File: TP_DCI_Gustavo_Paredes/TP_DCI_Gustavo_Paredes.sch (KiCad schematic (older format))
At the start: 30 parts, among them U101 LTC1485IS8PBF, U102 LTC1485IS8PBF, X701DB9F/101 DB9_Female, X702DB9M/101 DB9_Male

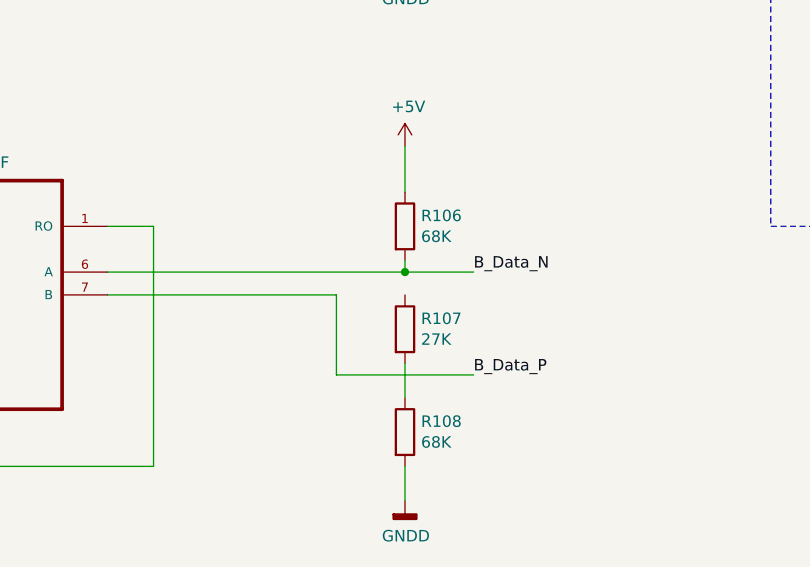
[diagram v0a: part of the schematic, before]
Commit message: Coneccion faltante.
Agregue una pequeña conexión faltante.
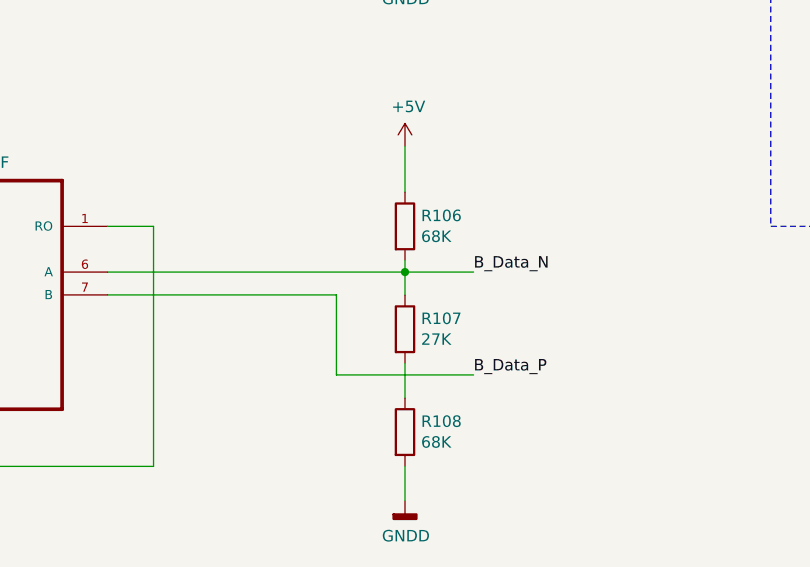
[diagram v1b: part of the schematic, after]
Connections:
- wire segments 150 -> 151
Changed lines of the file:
@@
 	0    -1   -1   0
 $EndComp
+Wire Wire Line
+	6300 3800 6300 3700
 Wire Bus Line
 	2250 1000 2250 4300

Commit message: Arreglo Etiqueta Global
Arregle la etiqueta global para que pase el ERC. Pero sigo con problemas en otros puntos.
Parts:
- C101, C102: footprint (none) -> Capacitor_THT:C_Disc_D3.0mm_W2.0mm_P2.50mm
- D101, D103, D104, D106, D107, D109, D110, D112: footprint (none) -> Diode_THT:D_DO-34_SOD68_P7.62mm_Horizontal
- D102, D105: footprint (none) -> Package_TO_SOT_SMD:SOT-23
- R101, R102, R103, R104, R105, R106, R107, R108, R109, R110, R111, R112: footprint (none) -> Resistor_THT:R_Axial_DIN0204_L3.6mm_D1.6mm_P5.08mm_Horizontal
- U101, U102: footprint SOIC127P600X175-8N -> LTC1485IS8PBF:SOIC127P600X175-8N
- X701DB9F/101: footprint (none) -> Connector_Dsub:DSUB-9_Female_Horizontal_P2.77x2.84mm_EdgePinOffset4.94mm_Housed_MountingHolesOffset7.48mm
- X702DB9M/101: footprint (none) -> Connector_Dsub:DSUB-9_Male_Horizontal_P2.77x2.84mm_EdgePinOffset4.94mm_Housed_MountingHolesOffset7.48mm
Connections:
- wire segments 151 -> 159
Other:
- note added: "Etiqueta Global\npara corregir ERC."
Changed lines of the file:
@@
 F 0 "X701DB9F/101" H 8520 1108 50  0000 C CNN
 F 1 "DB9_Female" H 8520 1199 50  0000 C CNN
-F 2 "" H 8600 1800 50  0001 C CNN
+F 2 "Connector_Dsub:DSUB-9_Female_Horizontal_P2.77x2.84mm_EdgePinOffset4.94mm_Housed_MountingHolesOffset7.48mm" H 8600 1800 50  0001 C CNN
 F 3 " ~" H 8600 1800 50  0001 C CNN
 	1    8600 1800
@@
 F 0 "R109" V 8843 2650 50  0000 C CNN
 F 1 "10R" V 8934 2650 50  0000 C CNN
-F 2 "" V 8980 2650 50  0001 C CNN
+F 2 "Resistor_THT:R_Axial_DIN0204_L3.6mm_D1.6mm_P5.08mm_Horizontal" V 8980 2650 50  0001 C CNN
 F 3 "~" H 9050 2650 50  0001 C CNN
 	1    9050 2650
@@
 F 0 "R111" V 9643 2650 50  0000 C CNN
 F 1 "10R" V 9734 2650 50  0000 C CNN
-F 2 "" V 9780 2650 50  0001 C CNN
+F 2 "Resistor_THT:R_Axial_DIN0204_L3.6mm_D1.6mm_P5.08mm_Horizontal" V 9780 2650 50  0001 C CNN
 F 3 "~" H 9850 2650 50  0001 C CNN
 	1    9850 2650
@@
 F 0 "R110" V 8843 3000 50  0000 C CNN
 F 1 "10R" V 8934 3000 50  0000 C CNN
-F 2 "" V 8980 3000 50  0001 C CNN
+F 2 "Resistor_THT:R_Axial_DIN0204_L3.6mm_D1.6mm_P5.08mm_Horizontal" V 8980 3000 50  0001 C CNN
 F 3 "~" H 9050 3000 50  0001 C CNN
 	1    9050 3000
@@
 F 0 "R112" V 9643 3000 50  0000 C CNN
 F 1 "10R" V 9734 3000 50  0000 C CNN
-F 2 "" V 9780 3000 50  0001 C CNN
+F 2 "Resistor_THT:R_Axial_DIN0204_L3.6mm_D1.6mm_P5.08mm_Horizontal" V 9780 3000 50  0001 C CNN
 F 3 "~" H 9850 3000 50  0001 C CNN
 	1    9850 3000
@@
 F 0 "R103" H 6370 1246 50  0000 L CNN
 F 1 "68K" H 6370 1155 50  0000 L CNN
-F 2 "" V 6230 1200 50  0001 C CNN
+F 2 "Resistor_THT:R_Axial_DIN0204_L3.6mm_D1.6mm_P5.08mm_Horizontal" V 6230 1200 50  0001 C CNN
 F 3 "~" H 6300 1200 50  0001 C CNN
 	1    6300 1200
@@
 F 0 "R104" H 6370 1696 50  0000 L CNN
 F 1 "27K" H 6370 1605 50  0000 L CNN
-F 2 "" V 6230 1650 50  0001 C CNN
+F 2 "Resistor_THT:R_Axial_DIN0204_L3.6mm_D1.6mm_P5.08mm_Horizontal" V 6230 1650 50  0001 C CNN
 F 3 "~" H 6300 1650 50  0001 C CNN
 	1    6300 1650
@@
 F 0 "R105" H 6370 2096 50  0000 L CNN
 F 1 "68K" H 6370 2005 50  0000 L CNN
-F 2 "" V 6230 2050 50  0001 C CNN
+F 2 "Resistor_THT:R_Axial_DIN0204_L3.6mm_D1.6mm_P5.08mm_Horizontal" V 6230 2050 50  0001 C CNN
 F 3 "~" H 6300 2050 50  0001 C CNN
 	1    6300 2050
@@
 F 0 "R106" H 6370 3546 50  0000 L CNN
 F 1 "68K" H 6370 3455 50  0000 L CNN
-F 2 "" V 6230 3500 50  0001 C CNN
+F 2 "Resistor_THT:R_Axial_DIN0204_L3.6mm_D1.6mm_P5.08mm_Horizontal" V 6230 3500 50  0001 C CNN
 F 3 "~" H 6300 3500 50  0001 C CNN
 	1    6300 3500
@@
 F 0 "R107" H 6370 3996 50  0000 L CNN
 F 1 "27K" H 6370 3905 50  0000 L CNN
-F 2 "" V 6230 3950 50  0001 C CNN
+F 2 "Resistor_THT:R_Axial_DIN0204_L3.6mm_D1.6mm_P5.08mm_Horizontal" V 6230 3950 50  0001 C CNN
 F 3 "~" H 6300 3950 50  0001 C CNN
 	1    6300 3950
@@
 F 0 "R108" H 6370 4446 50  0000 L CNN
 F 1 "68K" H 6370 4355 50  0000 L CNN
-F 2 "" V 6230 4400 50  0001 C CNN
+F 2 "Resistor_THT:R_Axial_DIN0204_L3.6mm_D1.6mm_P5.08mm_Horizontal" V 6230 4400 50  0001 C CNN
 F 3 "~" H 6300 4400 50  0001 C CNN
 	1    6300 4400
@@
 F 0 "X702DB9M/101" H 10070 1108 50  0000 C CNN
 F 1 "DB9_Male" H 10070 1199 50  0000 C CNN
-F 2 "" H 10150 1800 50  0001 C CNN
+F 2 "Connector_Dsub:DSUB-9_Male_Horizontal_P2.77x2.84mm_EdgePinOffset4.94mm_Housed_MountingHolesOffset7.48mm" H 10150 1800 50  0001 C CNN
 F 3 " ~" H 10150 1800 50  0001 C CNN
 	1    10150 1800
@@
 F 0 "D104" V 3396 6471 50  0000 R CNN
 F 1 "4,7V" V 3305 6471 50  0000 R CNN
-F 2 "" H 3350 6550 50  0001 C CNN
+F 2 "Diode_THT:D_DO-34_SOD68_P7.62mm_Horizontal" H 3350 6550 50  0001 C CNN
 F 3 "~" H 3350 6550 50  0001 C CNN
 	1    3350 6550
@@
 F 0 "D106" V 3804 6629 50  0000 L CNN
 F 1 "8,2V" V 3895 6629 50  0000 L CNN
-F 2 "" H 3850 6550 50  0001 C CNN
+F 2 "Diode_THT:D_DO-34_SOD68_P7.62mm_Horizontal" H 3850 6550 50  0001 C CNN
 F 3 "~" H 3850 6550 50  0001 C CNN
 	1    3850 6550
@@
 F 0 "D105" V 3304 7028 50  0000 L CNN
 F 1 "BAV99" V 3395 7028 50  0000 L CNN
-F 2 "" H 3350 6950 50  0001 C CNN
+F 2 "Package_TO_SOT_SMD:SOT-23" H 3350 6950 50  0001 C CNN
 F 3 "~" H 3350 6950 50  0001 C CNN
 	2    3350 6950
@@
 F 0 "R101" H 3020 2046 50  0000 L CNN
 F 1 "10K" H 3020 1955 50  0000 L CNN
-F 2 "" V 2880 2000 50  0001 C CNN
+F 2 "Resistor_THT:R_Axial_DIN0204_L3.6mm_D1.6mm_P5.08mm_Horizontal" V 2880 2000 50  0001 C CNN
 F 3 "~" H 2950 2000 50  0001 C CNN
 	1    2950 2000
@@
 F 0 "C101" V 3198 1000 50  0000 C CNN
 F 1 "22nF" V 3289 1000 50  0000 C CNN
-F 2 "" H 3488 850 50  0001 C CNN
+F 2 "Capacitor_THT:C_Disc_D3.0mm_W2.0mm_P2.50mm" H 3488 850 50  0001 C CNN
 F 3 "~" H 3450 1000 50  0001 C CNN
 	1    3450 1000
@@
 F 0 "U101" H 4300 1970 50  0000 C CNN
 F 1 "LTC1485IS8PBF" H 4300 1879 50  0000 C CNN
-F 2 "SOIC127P600X175-8N" H 4300 1400 50  0001 L BNN
+F 2 "LTC1485IS8PBF:SOIC127P600X175-8N" H 4300 1400 50  0001 L BNN
 F 3 "SOIC-8 Analog Devices" H 4300 1400 50  0001 L BNN
 F 4 "LTC1485IS8#PBF" H 4300 1400 50  0001 L BNN "Field4"
@@
 F 0 "R102" H 3020 4346 50  0000 L CNN
 F 1 "10K" H 3020 4255 50  0000 L CNN
-F 2 "" V 2880 4300 50  0001 C CNN
+F 2 "Resistor_THT:R_Axial_DIN0204_L3.6mm_D1.6mm_P5.08mm_Horizontal" V 2880 4300 50  0001 C CNN
 F 3 "~" H 2950 4300 50  0001 C CNN
 	1    2950 4300
@@
 F 0 "C102" V 3198 3300 50  0000 C CNN
 F 1 "22nF" V 3289 3300 50  0000 C CNN
-F 2 "" H 3488 3150 50  0001 C CNN
+F 2 "Capacitor_THT:C_Disc_D3.0mm_W2.0mm_P2.50mm" H 3488 3150 50  0001 C CNN
 F 3 "~" H 3450 3300 50  0001 C CNN
 	1    3450 3300
@@
 F 0 "U102" H 4300 4270 50  0000 C CNN
 F 1 "LTC1485IS8PBF" H 4300 4179 50  0000 C CNN
-F 2 "SOIC127P600X175-8N" H 4300 3700 50  0001 L BNN
+F 2 "LTC1485IS8PBF:SOIC127P600X175-8N" H 4300 3700 50  0001 L BNN
 F 3 "SOIC-8 Analog Devices" H 4300 3700 50  0001 L BNN
 F 4 "LTC1485IS8#PBF" H 4300 3700 50  0001 L BNN "Field4"
@@
 F 0 "D101" V 2396 6471 50  0000 R CNN
 F 1 "4,7V" V 2305 6471 50  0000 R CNN
-F 2 "" H 2350 6550 50  0001 C CNN
+F 2 "Diode_THT:D_DO-34_SOD68_P7.62mm_Horizontal" H 2350 6550 50  0001 C CNN
 F 3 "~" H 2350 6550 50  0001 C CNN
 	1    2350 6550
@@
 F 0 "D103" V 2804 6629 50  0000 L CNN
 F 1 "8,2V" V 2895 6629 50  0000 L CNN
-F 2 "" H 2850 6550 50  0001 C CNN
+F 2 "Diode_THT:D_DO-34_SOD68_P7.62mm_Horizontal" H 2850 6550 50  0001 C CNN
 F 3 "~" H 2850 6550 50  0001 C CNN
 	1    2850 6550
@@
 F 0 "D102" V 2304 7028 50  0000 L CNN
 F 1 "BAV99" V 2395 7028 50  0000 L CNN
-F 2 "" H 2350 6950 50  0001 C CNN
+F 2 "Package_TO_SOT_SMD:SOT-23" H 2350 6950 50  0001 C CNN
 F 3 "~" H 2350 6950 50  0001 C CNN
 	2    2350 6950
@@
 F 0 "D102" V 2896 6862 50  0000 R CNN
 F 1 "BAV99" V 2805 6862 50  0000 R CNN
-F 2 "" H 2850 6950 50  0001 C CNN
+F 2 "Package_TO_SOT_SMD:SOT-23" H 2850 6950 50  0001 C CNN
 F 3 "~" H 2850 6950 50  0001 C CNN
 	1    2850 6950
@@
 F 0 "D110" V 5596 6471 50  0000 R CNN
 F 1 "4,7V" V 5505 6471 50  0000 R CNN
-F 2 "" H 5550 6550 50  0001 C CNN
+F 2 "Diode_THT:D_DO-34_SOD68_P7.62mm_Horizontal" H 5550 6550 50  0001 C CNN
 F 3 "~" H 5550 6550 50  0001 C CNN
 	1    5550 6550
@@
 F 0 "D112" V 6004 6629 50  0000 L CNN
 F 1 "8,2V" V 6095 6629 50  0000 L CNN
-F 2 "" H 6050 6550 50  0001 C CNN
+F 2 "Diode_THT:D_DO-34_SOD68_P7.62mm_Horizontal" H 6050 6550 50  0001 C CNN
 F 3 "~" H 6050 6550 50  0001 C CNN
 	1    6050 6550
@@
 B_Data_P
 Wire Wire Line
-	5550 7150 5800 7150
-Wire Wire Line
 	5550 6800 5550 6700
 Wire Wire Line
 	6050 6700 6050 6800
-Wire Wire Line
-	5800 7150 5800 7250
-Connection ~ 5800 7150
-Wire Wire Line
-	5800 7150 6050 7150
 Wire Wire Line
 	6050 6400 6050 5900
@@
 F 0 "D107" V 4596 6471 50  0000 R CNN
 F 1 "4,7V" V 4505 6471 50  0000 R CNN
-F 2 "" H 4550 6550 50  0001 C CNN
+F 2 "Diode_THT:D_DO-34_SOD68_P7.62mm_Horizontal" H 4550 6550 50  0001 C CNN
 F 3 "~" H 4550 6550 50  0001 C CNN
 	1    4550 6550
@@
 F 0 "D109" V 5004 6629 50  0000 L CNN
 F 1 "8,2V" V 5095 6629 50  0000 L CNN
-F 2 "" H 5050 6550 50  0001 C CNN
+F 2 "Diode_THT:D_DO-34_SOD68_P7.62mm_Horizontal" H 5050 6550 50  0001 C CNN
 F 3 "~" H 5050 6550 50  0001 C CNN
 	1    5050 6550
@@
 Wire Wire Line
 	6300 3800 6300 3700
+$Comp
+L power:GNDPWR #PWR0121
+U 1 1 5D13F9B9
+P 6650 2350
+F 0 "#PWR0121" H 6650 2150 50  0001 C CNN
+F 1 "GNDPWR" H 6654 2196 50  0000 C CNN
+F 2 "" H 6650 2300 50  0001 C CNN
+F 3 "" H 6650 2300 50  0001 C CNN
+	1    6650 2350
+	1    0    0    -1
+$EndComp
+Wire Wire Line
+	6650 2350 6300 2350
+Connection ~ 6300 2350
+Wire Wire Line
+	5550 7150 5800 7150
+Wire Wire Line
+	5800 7250 5800 7150
+Connection ~ 5800 7150
+Wire Wire Line
+	5800 7150 6050 7150
+$Comp
+L power:GNDPWR #PWR0122
+U 1 1 5D14CE2D
+P 4250 7250
+F 0 "#PWR0122" H 4250 7050 50  0001 C CNN
+F 1 "GNDPWR" H 4254 7096 50  0000 C CNN
+F 2 "" H 4250 7200 50  0001 C CNN
+F 3 "" H 4250 7200 50  0001 C CNN
+	1    4250 7250
+	1    0    0    -1
+$EndComp
+Wire Wire Line
+	4250 7250 3600 7250
+Connection ~ 3600 7250
+Wire Wire Line
+	4800 7250 4250 7250
+Connection ~ 4800 7250
+Connection ~ 4250 7250
+$Comp
+L power:GNDPWR #PWR0123
+U 1 1 5D15A7B0
+P 6600 4700
+F 0 "#PWR0123" H 6600 4500 50  0001 C CNN
+F 1 "GNDPWR" H 6604 4546 50  0000 C CNN
+F 2 "" H 6600 4650 50  0001 C CNN
+F 3 "" H 6600 4650 50  0001 C CNN
+	1    6600 4700
+	1    0    0    -1
+$EndComp
+Wire Wire Line
+	6600 4700 6300 4700
+Connection ~ 6300 4700
+Wire Wire Line
+	5800 7250 4800 7250
+Connection ~ 5800 7250
+Wire Wire Line
+	3600 7250 2600 7250
+Connection ~ 2600 7250
+Text GLabel 950  1250 0    50   Output ~ 0
+P701
+Text Notes 600  1500 0    50   Italic 0
+Etiqueta Global\npara corregir ERC.
+Wire Wire Line
+	3500 2350 2950 2350
+Connection ~ 2950 2350
+Wire Wire Line
+	3500 4700 2950 4700
 Wire Bus Line
 	2250 1000 2250 4300
+Connection ~ 2950 4700
 $EndSCHEMATC

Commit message: Arreglos sugeridos x Docente
Realize los arreglos sugeridos por el Docente en la planilla.
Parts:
- added J101: Conector, symbol Connector:Conn_01x06_Male
- D101, D104, D107, D110: value 4,7V -> BZX84C4V7; LinkMouser (none) -> https://mouser.componentsearchengine.com/detail.html?search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; MouserPartNumber (none) -> 621-BZX84C4V7-7-F
- D102, D105, D108, D111: LinkMouser (none) -> https://mouser.componentsearchengine.com/detail.html?search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; MouserPartNumber (none) -> 863-NSVBAV99WT3G
- D103, D106, D109, D112: value 8,2V -> BZX84C8V2; LinkMouser (none) -> https://mouser.componentsearchengine.com/detail.html?search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; MouserPartNumber (none) -> 863-BZX84C8V2LT1G
- D108: LinkMouser (none) -> https://www.mouser.com/datasheet/2/308/BAV99WT1-D-101048.pdf; MouserPartNumber (none) -> 863-NSVBAV99WT3G
- J102: renamed from X701DB9F/101; value DB9_Female -> DB9 Hembra
- J103: renamed from X702DB9M/101; value DB9_Male -> DB9 Macho
- R109: footprint Resistor_THT:R_Axial_DIN0204_L3.6mm_D1.6mm_P5.08mm_Horizontal -> (none)
- R110, R111, R112: value 10R -> R; footprint Resistor_THT:R_Axial_DIN0204_L3.6mm_D1.6mm_P5.08mm_Horizontal -> (none)
- U101, U102: value LTC1485IS8PBF -> LTC1485; Descripcion (none) -> Line Transceiver 1TR 1 Transceiver 1 Receiver PDIP-8; Field4 LTC1485IS8#PBF -> (none); Field5 Line Transceiver 1TR 1 Transceiver 1 Receiver 8-Pin SOIC N -> (none); Field6 https://www.digikey.com.ar/product-detail/en/linear-technol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 -> (none); Field7 Analog Devices -> (none); Field8 LTC1485IS8#PBF-ND -> (none); LinkMouser (none) -> https://ar.mouser.com/ProductDetail/Analog-Devices/LTC1485C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; MouserPartNumber (none) -> 584-LTC1485CN8#PBF
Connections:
- net labels removed: GNDPWR, P701
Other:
- note added: "Differential Bus Transceiver"
- note added: "Protector Sobretensiones"
- note removed: "BZX84C4V7"
- note removed: "BZX84C8V2"
- note removed: "Etiqueta Global\npara corregir ERC."
- note removed: "RS485: LINE_A_SF, LINE_A_D0, LINE_A_D1\n LINE_B_SF, LINE_B_D0, LINE_B_D1"
- moved on the sheet: C101, C102, D101, D102A, D102B, D103, D104, D105A, D105B, D106, D108B, J102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

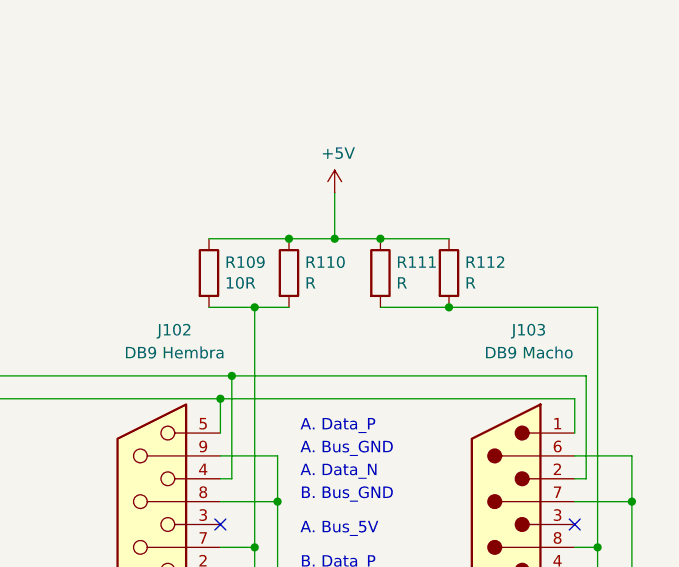
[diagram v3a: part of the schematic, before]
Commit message: Valores R/Huellas y Conector 6 Pines
Agregue valores a 3 R que faltaban, Huella de las mismas y del conector de 6 pines.
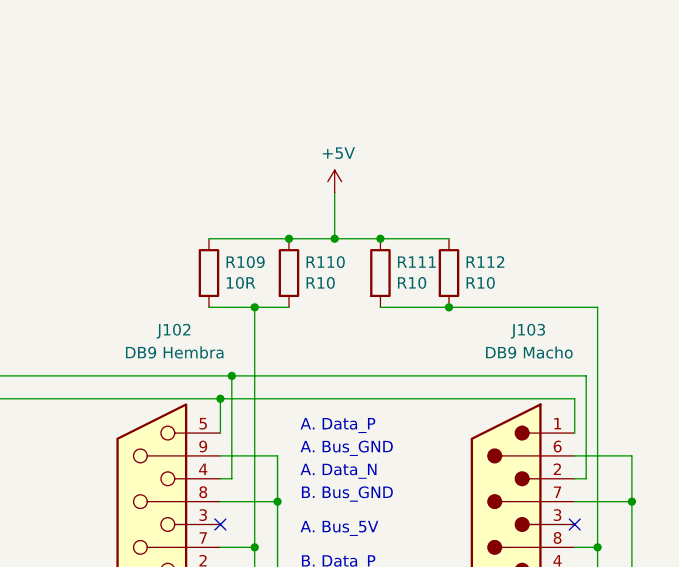
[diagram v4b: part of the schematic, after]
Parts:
- J101: footprint (none) -> Connector_PinHeader_1.00mm:PinHeader_1x06_P1.00mm_Vertical
- R109: footprint (none) -> Resistor_THT:R_Axial_DIN0204_L3.6mm_D1.6mm_P5.08mm_Horizontal
- R110, R111, R112: value R -> R10; footprint (none) -> Resistor_THT:R_Axial_DIN0204_L3.6mm_D1.6mm_P5.08mm_Horizontal
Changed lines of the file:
@@
 F 0 "R109" H 9220 2196 50  0000 L CNN
 F 1 "10R" H 9220 2105 50  0000 L CNN
-F 2 "" V 9080 2150 50  0001 C CNN
+F 2 "Resistor_THT:R_Axial_DIN0204_L3.6mm_D1.6mm_P5.08mm_Horizontal" V 9080 2150 50  0001 C CNN
 F 3 "~" H 9150 2150 50  0001 C CNN
 	1    9150 2150
@@
 P 9500 2150
 F 0 "R110" H 9570 2196 50  0000 L CNN
-F 1 "R" H 9570 2105 50  0000 L CNN
-F 2 "" V 9430 2150 50  0001 C CNN
+F 1 "R10" H 9570 2105 50  0000 L CNN
+F 2 "Resistor_THT:R_Axial_DIN0204_L3.6mm_D1.6mm_P5.08mm_Horizontal" V 9430 2150 50  0001 C CNN
 F 3 "~" H 9500 2150 50  0001 C CNN
 	1    9500 2150
@@
 P 10200 2150
 F 0 "R112" H 10270 2196 50  0000 L CNN
-F 1 "R" H 10270 2105 50  0000 L CNN
-F 2 "" V 10130 2150 50  0001 C CNN
+F 1 "R10" H 10270 2105 50  0000 L CNN
+F 2 "Resistor_THT:R_Axial_DIN0204_L3.6mm_D1.6mm_P5.08mm_Horizontal" V 10130 2150 50  0001 C CNN
 F 3 "~" H 10200 2150 50  0001 C CNN
 	1    10200 2150
@@
 P 9900 2150
 F 0 "R111" H 9970 2196 50  0000 L CNN
-F 1 "R" H 9970 2105 50  0000 L CNN
-F 2 "" V 9830 2150 50  0001 C CNN
+F 1 "R10" H 9970 2105 50  0000 L CNN
+F 2 "Resistor_THT:R_Axial_DIN0204_L3.6mm_D1.6mm_P5.08mm_Horizontal" V 9830 2150 50  0001 C CNN
 F 3 "~" H 9900 2150 50  0001 C CNN
 	1    9900 2150
@@
 F 0 "J101" H 750 3700 50  0000 C CNN
 F 1 "Conector" H 750 3600 50  0000 C CNN
-F 2 "" H 650 3200 50  0001 C CNN
+F 2 "Connector_PinHeader_1.00mm:PinHeader_1x06_P1.00mm_Vertical" H 650 3200 50  0001 C CNN
 F 3 "~" H 650 3200 50  0001 C CNN
 	1    650  3200

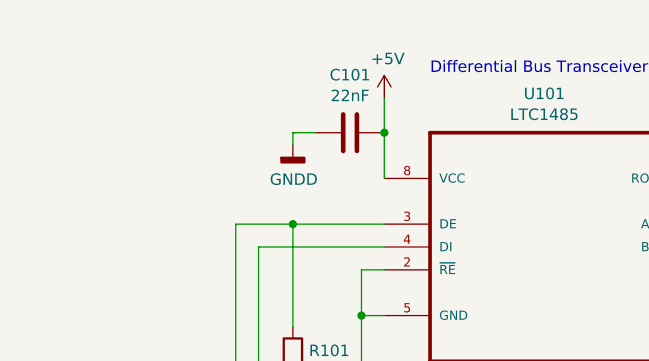
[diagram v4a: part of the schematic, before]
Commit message: Agregue Conector VCC
Agregue conector para 5V y GND. Ya esta hecha la distribucion basica de componentes en el PCB. Recargo la NETList.
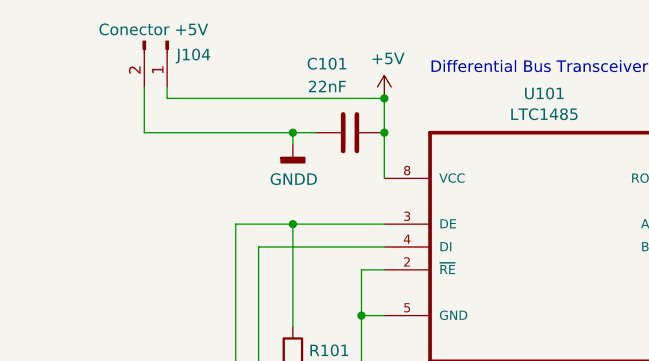
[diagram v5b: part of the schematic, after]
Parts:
- added J104: Conector +5V, Connector_PinHeader_1.00mm:PinHeader_1x02_P1.00mm_Vertical, symbol Connector:Conn_01x02_Male
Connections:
- net +5V: now also J104.1 (Pin_1)
- net GNDD: now also J104.2 (Pin_2)
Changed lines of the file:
@@
 U 1 1 5D118BBC
 P 2000 1200
-F 0 "C101" V 1748 1200 50  0000 C CNN
-F 1 "22nF" V 1839 1200 50  0000 C CNN
+F 0 "C101" V 1700 1100 50  0000 C CNN
+F 1 "22nF" V 1800 1100 50  0000 C CNN
 F 2 "Capacitor_THT:C_Disc_D3.0mm_W2.0mm_P2.50mm" H 2038 1050 50  0001 C CNN
 F 3 "~" H 2000 1200 50  0001 C CNN
@@
 Wire Wire Line
 	3550 1400 3550 3200
+$Comp
+L Connector:Conn_01x02_Male J104
+U 1 1 5D4086E9
+P 1200 800
+F 0 "J104" V 1260 841 50  0000 L CNN
+F 1 "Conector +5V" V 1150 500 50  0000 L CNN
+F 2 "Connector_PinHeader_1.00mm:PinHeader_1x02_P1.00mm_Vertical" H 1200 800 50  0001 C CNN
+F 3 "~" H 1200 800 50  0001 C CNN
+	1    1200 800
+	0    1    1    0
+$EndComp
+Wire Wire Line
+	2150 1050 1200 1050
+Wire Wire Line
+	1200 1050 1200 1000
+Connection ~ 2150 1050
+Wire Wire Line
+	1750 1200 1100 1200
+Wire Wire Line
+	1100 1200 1100 1000
+Connection ~ 1750 1200
 $EndSCHEMATC
